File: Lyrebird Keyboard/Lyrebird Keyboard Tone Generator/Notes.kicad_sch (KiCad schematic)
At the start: 78 parts, among them IC15 MC14024BDG, IC16 MC14024BDG, IC17 MC14024BDG, IC18 MC14024BDG, IC19 MC14024BDG, IC20 MC14024BDG

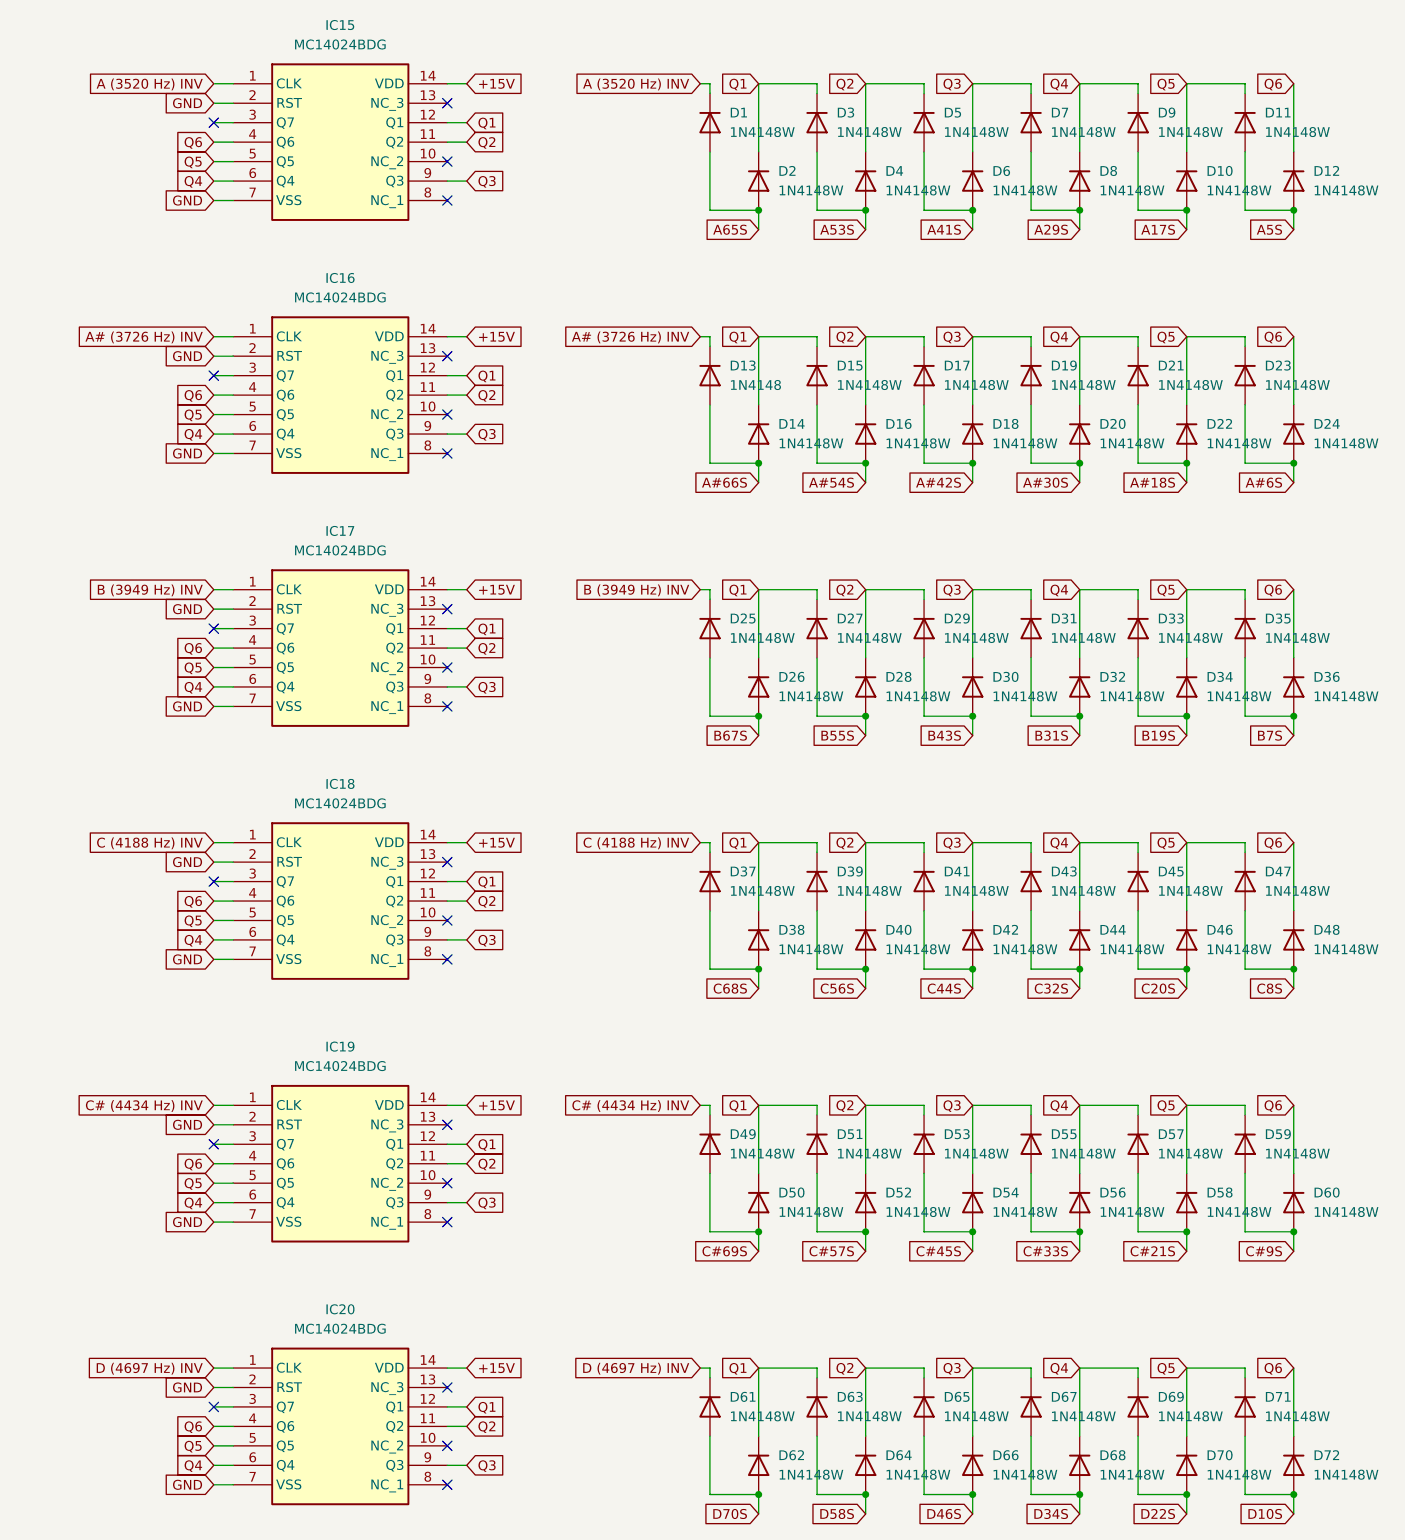
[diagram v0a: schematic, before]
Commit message: Further Tone Generator Work, Diode mixers placed
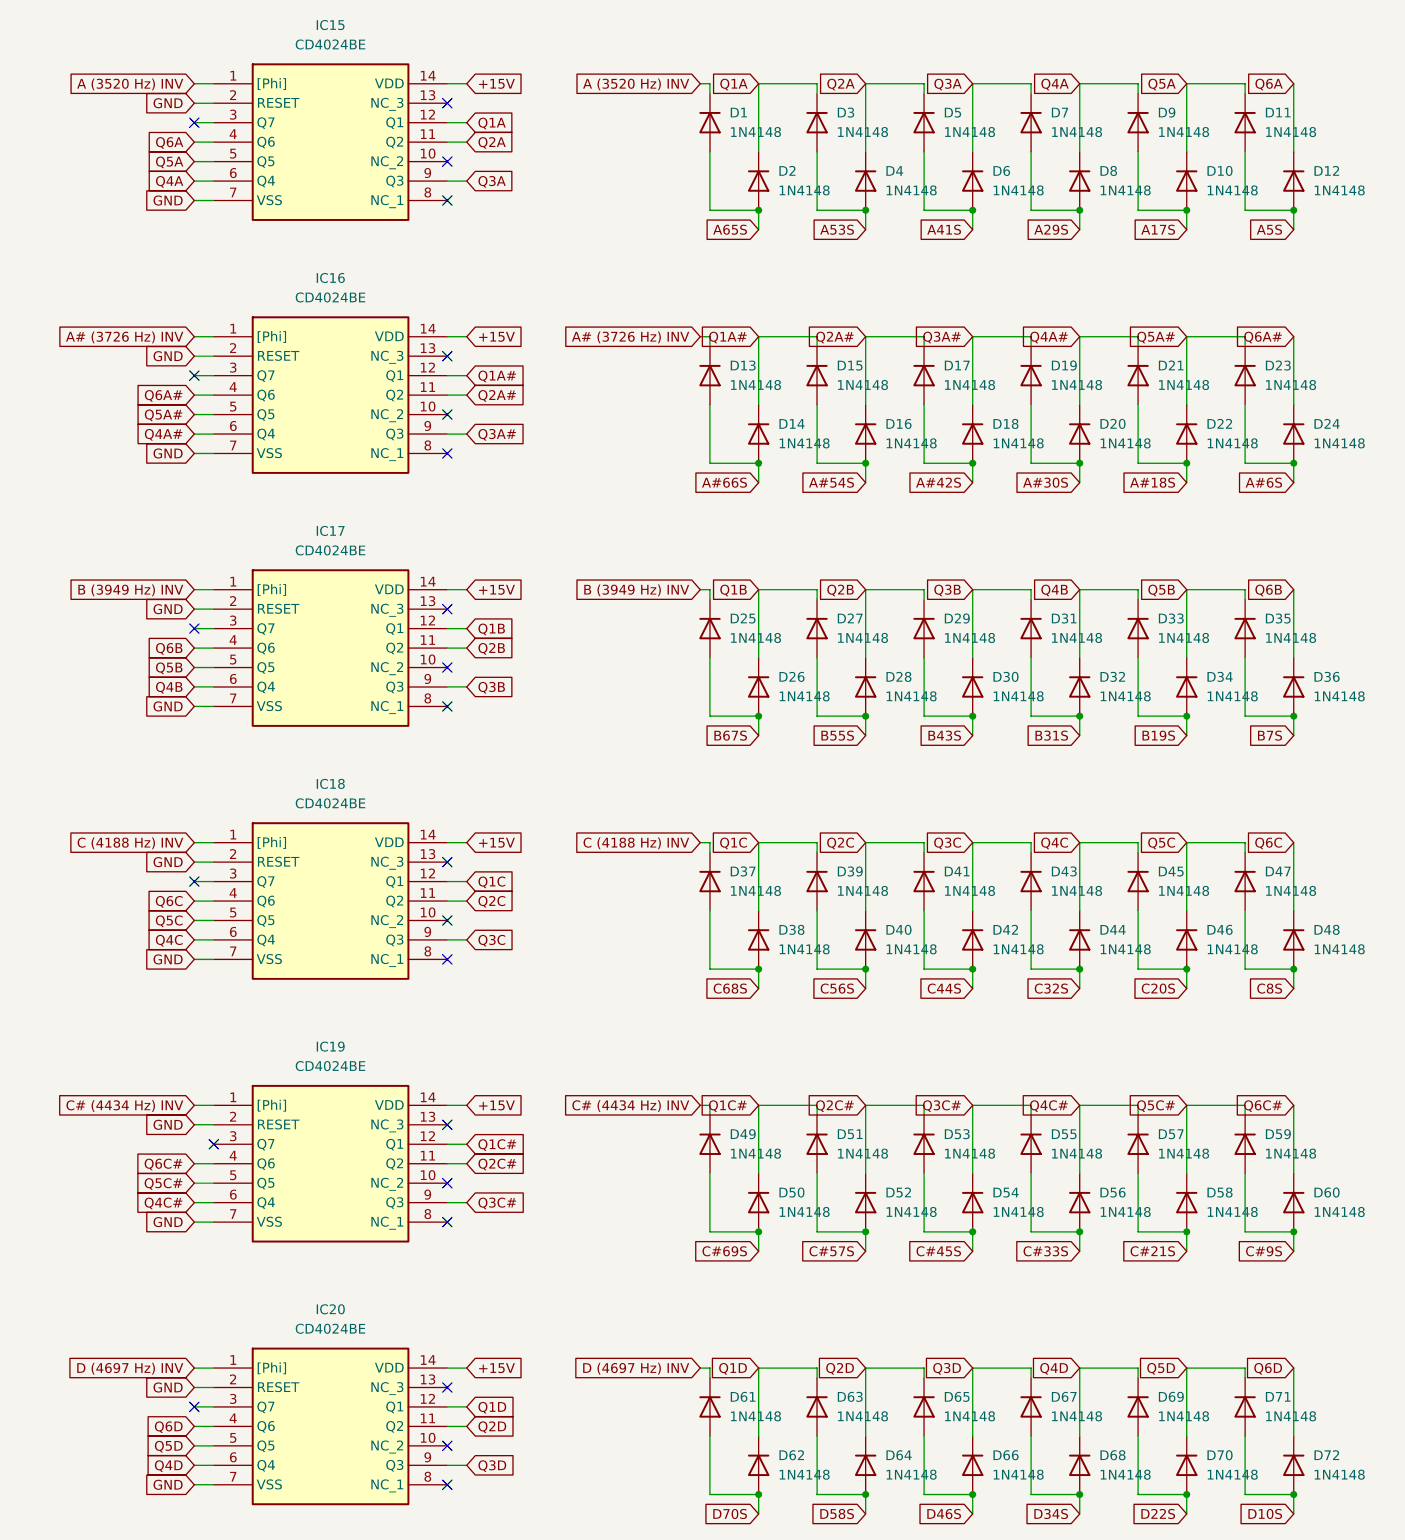
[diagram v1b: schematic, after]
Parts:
- removed D1, D10, D11, D12, D14, D15, D16, D17, D18, D19, D2, D20, D21, D22, D23, D24, D25, D26, D27, D28, D29, D3, D30, D31, D32, D33, D34, D35, D36, D37, D38, D39, D4, D40, D41, D42, D43, D44, D45, D46, D47, D48, D49, D5, D50, D51, D52, D53, D54, D55, D56, D57, D58, D59, D6, D60, D61, D62, D63, D64, D65, D66, D67, D68, D69, D7, D70, D71, D72, D8, D9: 1N4148W, Diode_SMD:D_SOD-123, symbol Diode:1N4148W
- removed IC15, IC16, IC17, IC18, IC19, IC20: MC14024BDG, SOIC127P600X175-14N, symbol SamacSys_Parts:MC14024BDG
- added D1, D10, D11, D12, D14, D15, D16, D17, D18, D19, D2, D20, D21, D22, D23, D24, D25, D26, D27, D28, D29, D3, D30, D31, D32, D33, D34, D35, D36, D37, D38, D39, D4, D40, D41, D42, D43, D44, D45, D46, D47, D48, D49, D5, D50, D51, D52, D53, D54, D55, D56, D57, D58, D59, D6, D60, D61, D62, D63, D64, D65, D66, D67, D68, D69, D7, D70, D71, D72, D8, D9: 1N4148, Diode_THT:D_DO-35_SOD27_P7.62mm_Horizontal, symbol Diode:1N4148
- added IC15, IC16, IC17, IC18, IC19, IC20: CD4024BE, DIP794W53P254L1930H508Q14N, symbol SamacSys_Parts:CD4024BE
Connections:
- net +15V: now also IC15.14 (VDD), IC16.14 (VDD), IC17.14 (VDD), IC18.14 (VDD), IC19.14 (VDD), IC20.14 (VDD)
- net A (3520 Hz) INV: now also D1.1 (K), IC15.1 ([Phi])
- net A# (3726 Hz) INV: now also IC16.1 ([Phi])
- net A#18S: now also D21.2 (A), D22.2 (A)
- net A#30S: now also D19.2 (A), D20.2 (A)
- net A#42S: now also D17.2 (A), D18.2 (A)
- net A#54S: now also D15.2 (A), D16.2 (A)
- net A#66S: now also D14.2 (A)
- net A#6S: now also D23.2 (A), D24.2 (A)
- net A17S: now also D10.2 (A), D9.2 (A)
- net A29S: now also D7.2 (A), D8.2 (A)
- net A41S: now also D5.2 (A), D6.2 (A)
- net A53S: now also D3.2 (A), D4.2 (A)
- net A5S: now also D11.2 (A), D12.2 (A)
- net A65S: now also D1.2 (A), D2.2 (A)
- net B (3949 Hz) INV: now also D25.1 (K), IC17.1 ([Phi])
- net B19S: now also D33.2 (A), D34.2 (A)
- net B31S: now also D31.2 (A), D32.2 (A)
- net B43S: now also D29.2 (A), D30.2 (A)
- net B55S: now also D27.2 (A), D28.2 (A)
- net B67S: now also D25.2 (A), D26.2 (A)
- net B7S: now also D35.2 (A), D36.2 (A)
- net C (4188 Hz) INV: now also D37.1 (K), IC18.1 ([Phi])
- net C# (4434 Hz) INV: now also D49.1 (K), IC19.1 ([Phi])
- net C#21S: now also D57.2 (A), D58.2 (A)
- net C#33S: now also D55.2 (A), D56.2 (A)
- net C#45S: now also D53.2 (A), D54.2 (A)
- net C#57S: now also D51.2 (A), D52.2 (A)
- net C#69S: now also D49.2 (A), D50.2 (A)
- net C#9S: now also D59.2 (A), D60.2 (A)
- net C20S: now also D45.2 (A), D46.2 (A)
- net C32S: now also D43.2 (A), D44.2 (A)
- net C44S: now also D41.2 (A), D42.2 (A)
- net C56S: now also D39.2 (A), D40.2 (A)
- net C68S: now also D37.2 (A), D38.2 (A)
- net C8S: now also D47.2 (A), D48.2 (A)
- net D (4697 Hz) INV: now also D61.1 (K), IC20.1 ([Phi])
- net D10S: now also D71.2 (A), D72.2 (A)
- net D22S: now also D69.2 (A), D70.2 (A)
- net D34S: now also D67.2 (A), D68.2 (A)
- net D46S: now also D65.2 (A), D66.2 (A)
- net D58S: now also D63.2 (A), D64.2 (A)
- net D70S: now also D61.2 (A), D62.2 (A)
- net GND: now also IC15.2 (RESET), IC15.7 (VSS), IC16.2 (RESET), IC16.7 (VSS), IC17.2 (RESET), IC17.7 (VSS), IC18.2 (RESET), IC18.7 (VSS), IC19.2 (RESET), IC19.7 (VSS), IC20.2 (RESET), IC20.7 (VSS)
- new net Q1A: D2.1 (K), D3.1 (K), IC15.12 (Q1)
- new net Q1A#: D14.1 (K), D15.1 (K), IC16.12 (Q1)
- new net Q1B: D26.1 (K), D27.1 (K), IC17.12 (Q1)
- new net Q1C: D38.1 (K), D39.1 (K), IC18.12 (Q1)
- new net Q1C#: D50.1 (K), D51.1 (K), IC19.12 (Q1)
- new net Q1D: D62.1 (K), D63.1 (K), IC20.12 (Q1)
- new net Q2A: D4.1 (K), D5.1 (K), IC15.11 (Q2)
- new net Q2A#: D16.1 (K), D17.1 (K), IC16.11 (Q2)
- new net Q2B: D28.1 (K), D29.1 (K), IC17.11 (Q2)
- new net Q2C: D40.1 (K), D41.1 (K), IC18.11 (Q2)
- new net Q2C#: D52.1 (K), D53.1 (K), IC19.11 (Q2)
- new net Q2D: D64.1 (K), D65.1 (K), IC20.11 (Q2)
- new net Q3A: D6.1 (K), D7.1 (K), IC15.9 (Q3)
- new net Q3A#: D18.1 (K), D19.1 (K), IC16.9 (Q3)
- new net Q3B: D30.1 (K), D31.1 (K), IC17.9 (Q3)
- new net Q3C: D42.1 (K), D43.1 (K), IC18.9 (Q3)
- new net Q3C#: D54.1 (K), D55.1 (K), IC19.9 (Q3)
- new net Q3D: D66.1 (K), D67.1 (K), IC20.9 (Q3)
- new net Q4A: D8.1 (K), D9.1 (K), IC15.6 (Q4)
- new net Q4A#: D20.1 (K), D21.1 (K), IC16.6 (Q4)
- new net Q4B: D32.1 (K), D33.1 (K), IC17.6 (Q4)
- new net Q4C: D44.1 (K), D45.1 (K), IC18.6 (Q4)
- new net Q4C#: D56.1 (K), D57.1 (K), IC19.6 (Q4)
- new net Q4D: D68.1 (K), D69.1 (K), IC20.6 (Q4)
- new net Q5A: D10.1 (K), D11.1 (K), IC15.5 (Q5)
- new net Q5A#: D22.1 (K), D23.1 (K), IC16.5 (Q5)
- new net Q5B: D34.1 (K), D35.1 (K), IC17.5 (Q5)
- new net Q5C: D46.1 (K), D47.1 (K), IC18.5 (Q5)
- new net Q5C#: D58.1 (K), D59.1 (K), IC19.5 (Q5)
- new net Q5D: D70.1 (K), D71.1 (K), IC20.5 (Q5)
- new net Q6A: D12.1 (K), IC15.4 (Q6)
- new net Q6A#: D24.1 (K), IC16.4 (Q6)
- new net Q6B: D36.1 (K), IC17.4 (Q6)
- new net Q6C: D48.1 (K), IC18.4 (Q6)
- new net Q6C#: D60.1 (K), IC19.4 (Q6)
- new net Q6D: D72.1 (K), IC20.4 (Q6)
